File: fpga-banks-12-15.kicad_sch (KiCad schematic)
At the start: 1 part, among them U3002 XC7K160T-FFG676

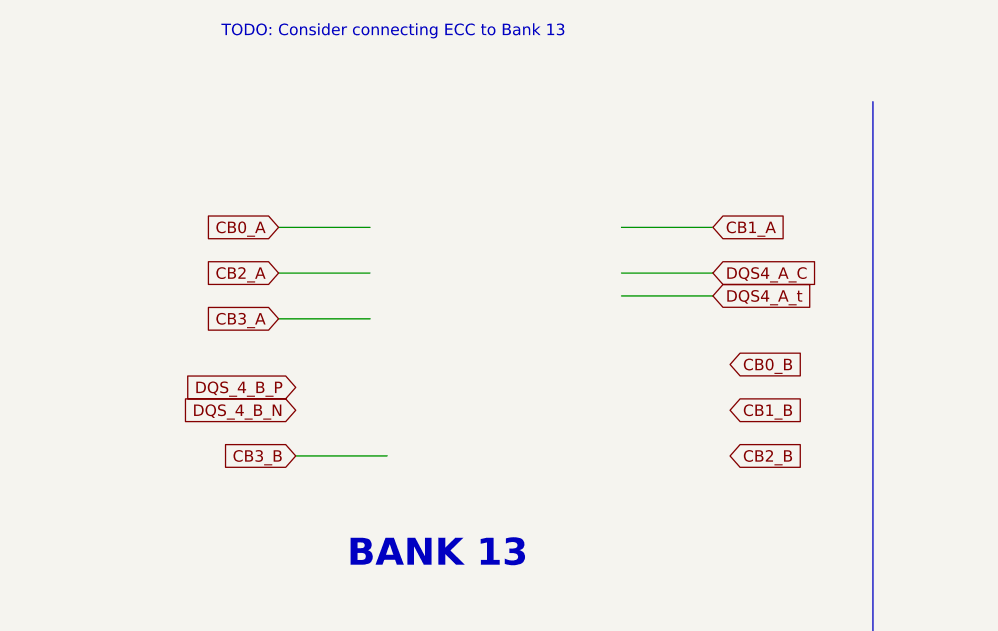
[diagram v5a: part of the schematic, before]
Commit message: Improve DDR assigment, connect ECC to remaining pins, cleanup not used components, continue placement of misc. components
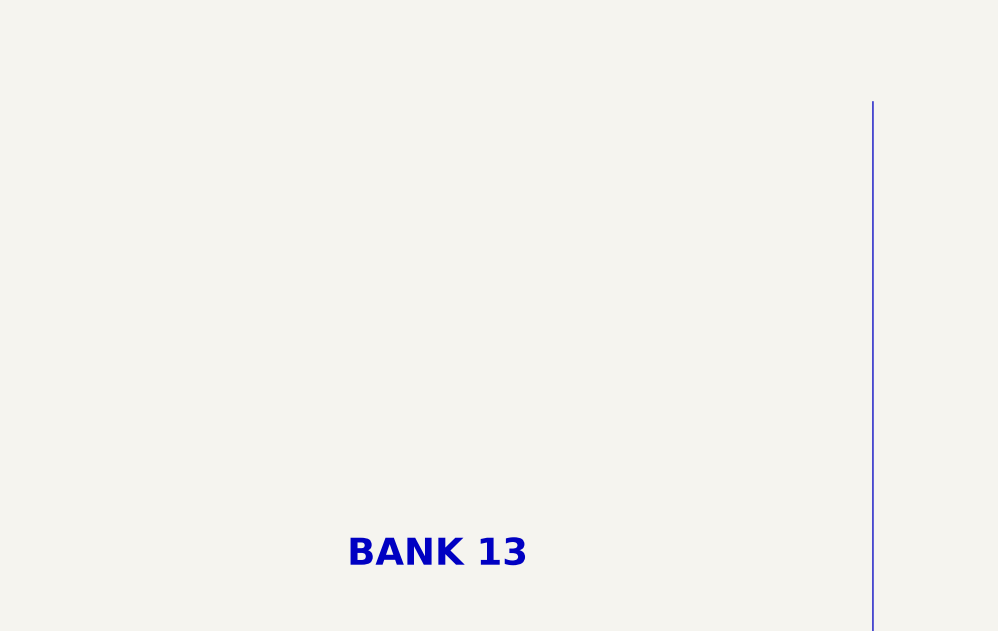
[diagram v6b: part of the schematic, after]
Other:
- note removed: "TODO: Consider connecting ECC to Bank 13"
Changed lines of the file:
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@@
-    (stroke (width 0) (type default) (color 0 0 0 0))
-  )
-  (wire (pts (xy 182.245 31.115) (xy 192.405 31.115))
     (stroke (width 0) (type default) (color 0 0 0 0))
   )
@@
     (stroke (width 0) (type default) (color 0 0 0 0))
   )
-  (wire (pts (xy 182.245 33.655) (xy 192.405 33.655))
-    (stroke (width 0) (type default) (color 0 0 0 0))
-  )
   (wire (pts (xy 241.3 104.775) (xy 245.11 104.775))
     (stroke (width 0) (type default) (color 0 0 0 0))
@@
     (stroke (width 0) (type default) (color 0 0 0 0))
   )
-  (wire (pts (xy 146.05 51.435) (xy 156.21 51.435))
-    (stroke (width 0) (type default) (color 0 0 0 0))
-  )
   (wire (pts (xy 241.3 112.395) (xy 245.11 112.395))
     (stroke (width 0) (type default) (color 0 0 0 0))
@@
     (stroke (width 0) (type default) (color 0 0 0 0))
   )
-  (wire (pts (xy 144.145 31.115) (xy 154.305 31.115))
-    (stroke (width 0) (type default) (color 0 0 0 0))
-  )
   (wire (pts (xy 64.77 208.915) (xy 68.58 208.915))
     (stroke (width 0) (type default) (color 0 0 0 0))
@@
     (stroke (width 0) (type default) (color 0 0 0 0))
   )
-  (wire (pts (xy 154.305 26.035) (xy 144.145 26.035))
-    (stroke (width 0) (type default) (color 0 0 0 0))
-  )
   (wire (pts (xy 241.3 173.355) (xy 245.11 173.355))
     (stroke (width 0) (type default) (color 0 0 0 0))
@@
     (stroke (width 0) (type default) (color 0 0 0 0))
   )
-  (wire (pts (xy 144.145 36.195) (xy 154.305 36.195))
-    (stroke (width 0) (type default) (color 0 0 0 0))
-  )
   (wire (pts (xy 64.77 203.835) (xy 68.58 203.835))
     (stroke (width 0) (type default) (color 0 0 0 0))
@@
   )
   (wire (pts (xy 64.77 109.855) (xy 68.58 109.855))
-    (stroke (width 0) (type default) (color 0 0 0 0))
-  )
-  (wire (pts (xy 182.245 26.035) (xy 192.405 26.035))
     (stroke (width 0) (type default) (color 0 0 0 0))
   )
@@
     (effects (font (size 2.9972 2.9972) (thickness 0.5994) bold) (justify left bottom))
   )
-  (text "TODO: Consider connecting ECC to Bank 13" (at 137.795 5.08 0)
-    (effects (font (size 1.27 1.27)) (justify left bottom))
-  )
   (text "BANK 15" (at 335.915 64.135 0)
     (effects (font (size 2.9972 2.9972) (thickness 0.5994) bold) (justify left bottom))
@@
     )
   )
-  (global_label "DQS_4_B_P" (shape input) (at 146.05 43.815 180) (fields_autoplaced)
-    (effects (font (size 1.27 1.27)) (justify right))
-    (property "Intersheet References" "${INTERSHEET_REFS}" (id 0) (at 133.2634 43.8944 0)
-      (effects (font (size 1.27 1.27)) (justify right) hide)
-    )
-  )
   (global_label "HOT_SWAP_GREEN" (shape input) (at 241.3 145.415 180) (fields_autoplaced)
     (effects (font (size 1.27 1.27)) (justify right))
@@
     )
   )
-  (global_label "CB0_B" (shape input) (at 194.31 41.275 0) (fields_autoplaced)
-    (effects (font (size 1.27 1.27)) (justify left))
-    (property "Intersheet References" "${INTERSHEET_REFS}" (id 0) (at 202.6213 41.1956 0)
-      (effects (font (size 1.27 1.27)) (justify left) hide)
-    )
-  )
   (global_label "ETH_RXD1" (shape input) (at 64.77 114.935 180) (fields_autoplaced)
     (effects (font (size 1.27 1.27)) (justify right))
@@
     (property "Intersheet References" "${INTERSHEET_REFS}" (id 0) (at 5.08 0 0)
       (effects (font (size 1.27 1.27)) hide)
-    )
-  )
-  (global_label "CB1_B" (shape input) (at 194.31 46.355 0) (fields_autoplaced)
-    (effects (font (size 1.27 1.27)) (justify left))
-    (property "Intersheet References" "${INTERSHEET_REFS}" (id 0) (at 202.6213 46.2756 0)
-      (effects (font (size 1.27 1.27)) (justify left) hide)
     )
   )
@@
     )
   )
-  (global_label "CB2_B" (shape input) (at 194.31 51.435 0) (fields_autoplaced)
-    (effects (font (size 1.27 1.27)) (justify left))
-    (property "Intersheet References" "${INTERSHEET_REFS}" (id 0) (at 202.6213 51.3556 0)
-      (effects (font (size 1.27 1.27)) (justify left) hide)
-    )
-  )
   (global_label "FPGA_VTT_CNTL" (shape input) (at 241.3 183.515 180) (fields_autoplaced)
     (effects (font (size 1.27 1.27)) (justify right))
@@
     )
   )
-  (global_label "CB3_B" (shape input) (at 146.05 51.435 180) (fields_autoplaced)
-    (effects (font (size 1.27 1.27)) (justify right))
-    (property "Intersheet References" "${INTERSHEET_REFS}" (id 0) (at 137.7387 51.5144 0)
-      (effects (font (size 1.27 1.27)) (justify right) hide)
-    )
-  )
   (global_label "AUX_JTAG_TCK" (shape input) (at 241.3 122.555 180) (fields_autoplaced)
     (effects (font (size 1.27 1.27)) (justify right))
@@
     )
   )
-  (global_label "DQS4_A_t" (shape input) (at 192.405 33.655 0) (fields_autoplaced)
-    (effects (font (size 1.27 1.27)) (justify left))
-    (property "Intersheet References" "${INTERSHEET_REFS}" (id 0) (at 203.4982 33.5756 0)
-      (effects (font (size 1.27 1.27)) (justify left) hide)
-    )
-  )
   (global_label "ETH_MDIO" (shape input) (at 64.77 135.255 180) (fields_autoplaced)
     (effects (font (size 1.27 1.27)) (justify right))
@@
     )
   )
-  (global_label "CB3_A" (shape input) (at 144.145 36.195 180) (fields_autoplaced)
-    (effects (font (size 1.27 1.27)) (justify right))
-    (property "Intersheet References" "${INTERSHEET_REFS}" (id 0) (at 136.0151 36.2744 0)
-      (effects (font (size 1.27 1.27)) (justify right) hide)
-    )
-  )
   (global_label "QSPI_DQ2" (shape input) (at 241.3 99.695 180) (fields_autoplaced)
     (effects (font (size 1.27 1.27)) (justify right))
@@
     )
   )
-  (global_label "CB1_A" (shape input) (at 192.405 26.035 0) (fields_autoplaced)
-    (effects (font (size 1.27 1.27)) (justify left))
-    (property "Intersheet References" "${INTERSHEET_REFS}" (id 0) (at 200.5349 25.9556 0)
-      (effects (font (size 1.27 1.27)) (justify left) hide)
-    )
-  )
   (global_label "HR_DQ7" (shape input) (at 64.77 173.355 180) (fields_autoplaced)
     (effects (font (size 1.27 1.27)) (justify right))
@@
     )
   )
-  (global_label "CB0_A" (shape input) (at 144.145 26.035 180) (fields_autoplaced)
-    (effects (font (size 1.27 1.27)) (justify right))
-    (property "Intersheet References" "${INTERSHEET_REFS}" (id 0) (at 136.0151 26.1144 0)
-      (effects (font (size 1.27 1.27)) (justify right) hide)
-    )
-  )
   (global_label "ETH_TXD1" (shape input) (at 64.77 142.875 180) (fields_autoplaced)
     (effects (font (size 1.27 1.27)) (justify right))
@@
     )
   )
-  (global_label "DQS_4_B_N" (shape input) (at 146.05 46.355 180) (fields_autoplaced)
-    (effects (font (size 1.27 1.27)) (justify right))
-    (property "Intersheet References" "${INTERSHEET_REFS}" (id 0) (at 133.2029 46.4344 0)
-      (effects (font (size 1.27 1.27)) (justify right) hide)
-    )
-  )
   (global_label "HR_DQ4" (shape input) (at 64.77 203.835 180) (fields_autoplaced)
     (effects (font (size 1.27 1.27)) (justify right))
@@
     )
   )
-  (global_label "CB2_A" (shape input) (at 144.145 31.115 180) (fields_autoplaced)
-    (effects (font (size 1.27 1.27)) (justify right))
-    (property "Intersheet References" "${INTERSHEET_REFS}" (id 0) (at 136.0151 31.1944 0)
-      (effects (font (size 1.27 1.27)) (justify right) hide)
-    )
-  )
-  (global_label "DQS4_A_C" (shape input) (at 192.405 31.115 0) (fields_autoplaced)
-    (effects (font (size 1.27 1.27)) (justify left))
-    (property "Intersheet References" "${INTERSHEET_REFS}" (id 0) (at 204.0425 31.0356 0)
-      (effects (font (size 1.27 1.27)) (justify left) hide)
-    )
-  )

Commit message: Add loclib
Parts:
- U3002: footprint data-center-rdimm-ddr4-tester-footprints:BGA-676_27x27mm_Layout26x26_P1X1mm -> sodimm-ddr5-tester-footprints:BGA-676_27x27mm_Layout26x26_P1X1mm; symbol data-center-rdimm-ddr4-tester:XC7K160T-FFG676 -> sodimm-ddr5-tester:XC7K160T-FFG676
